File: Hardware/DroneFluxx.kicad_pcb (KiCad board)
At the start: 4 copper layers, 45 x 45 mm, 58 parts, among them J1 Conn_01x04_Male, J2 Conn_01x02_Female, J20 Conn_01x01_Female, J21 Conn_01x01_Female, J22 Conn_01x01_Female, U1 BMP388, U2 LSM6DSM, U3 LP2985-3.3, U4 LIS3MDL, U5 CAM-M8C-0, U6 STM32F410RBTx

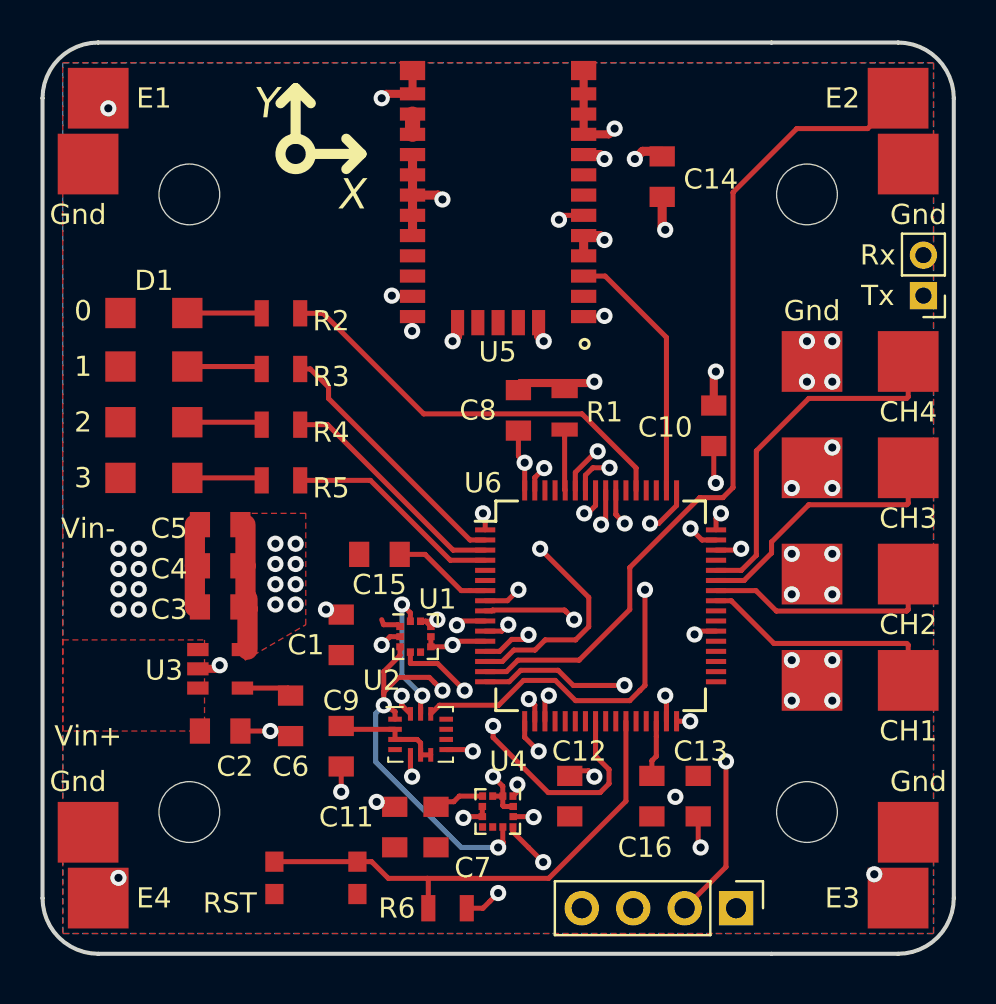
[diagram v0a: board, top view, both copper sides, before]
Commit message: Updated hardware to use latest library references.
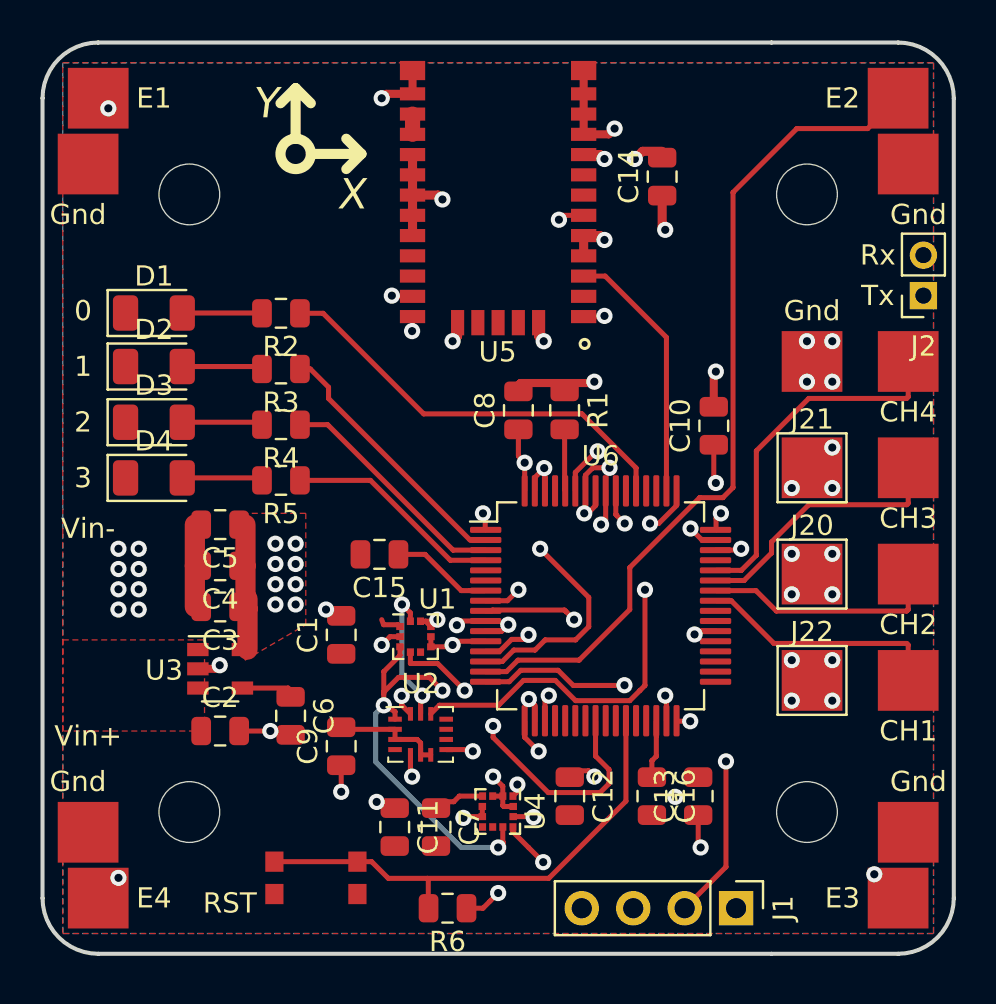
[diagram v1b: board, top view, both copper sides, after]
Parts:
- C1, C10, C11, C12, C13, C14, C15, C16, C2, C3, C4, C5, C6, C7, C8, C9: footprint MyLibs:C_0805 -> Capacitor_SMD:C_0805_2012Metric
- D1, D2, D3, D4: footprint LEDs:LED_1206 -> LED_SMD:LED_1206_3216Metric
- G***: footprint Logo:flight -> kyleRhess_logos:logo_foxflight
- G***: footprint Logo:fox -> kyleRhess_logos:logo_foxhound
- G***: footprint Logo:logo -> kyleRhess_logos:logo_blackmesa
- J1: footprint Pin_Headers:Pin_Header_Straight_1x04_Pitch2.54mm -> Connector_PinHeader_2.54mm:PinHeader_1x04_P2.54mm_Vertical
- J2: footprint Pin_Headers:Pin_Header_Straight_1x02_Pitch2.00mm -> Connector_PinSocket_2.00mm:PinSocket_1x02_P2.00mm_Vertical
- J20, J21, J22: footprint Measurement_Points:Measurement_Point_Square-SMD-Pad_Big -> TestPoint:TestPoint_Pad_3.0x3.0mm
- R1, R2, R3, R4, R5, R6: footprint MyLibs:R_0805 -> Resistor_SMD:R_0805_2012Metric
- U1: footprint MyLibs:LGA-10_2x2mm_Pitch0.5mm -> kyleRhess_packages:LGA-10_2x2mm_Pitch0.5mm
- U2: footprint Housings_LGA:Bosch_LGA-14_3x2.5mm_Pitch0.5mm -> Package_LGA:Bosch_LGA-14_3x2.5mm_P0.5mm
- U3: footprint TO_SOT_Packages_SMD:SOT-23-5 -> Package_TO_SOT_SMD:SOT-23-5
- U4: footprint Housings_LGA:LGA-12_2x2mm_Pitch0.5mm -> Package_LGA:LGA-12_2x2mm_P0.5mm
- U5: footprint MyLibs:31-SMD Module -> kyleRhess_packages:31-SMD_Module
- U6: footprint Housings_QFP:LQFP-64_10x10mm_Pitch0.5mm -> Package_QFP:LQFP-64_10x10mm_P0.5mm
